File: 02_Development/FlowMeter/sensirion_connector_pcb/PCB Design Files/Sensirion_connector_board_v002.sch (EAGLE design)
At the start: 13 parts

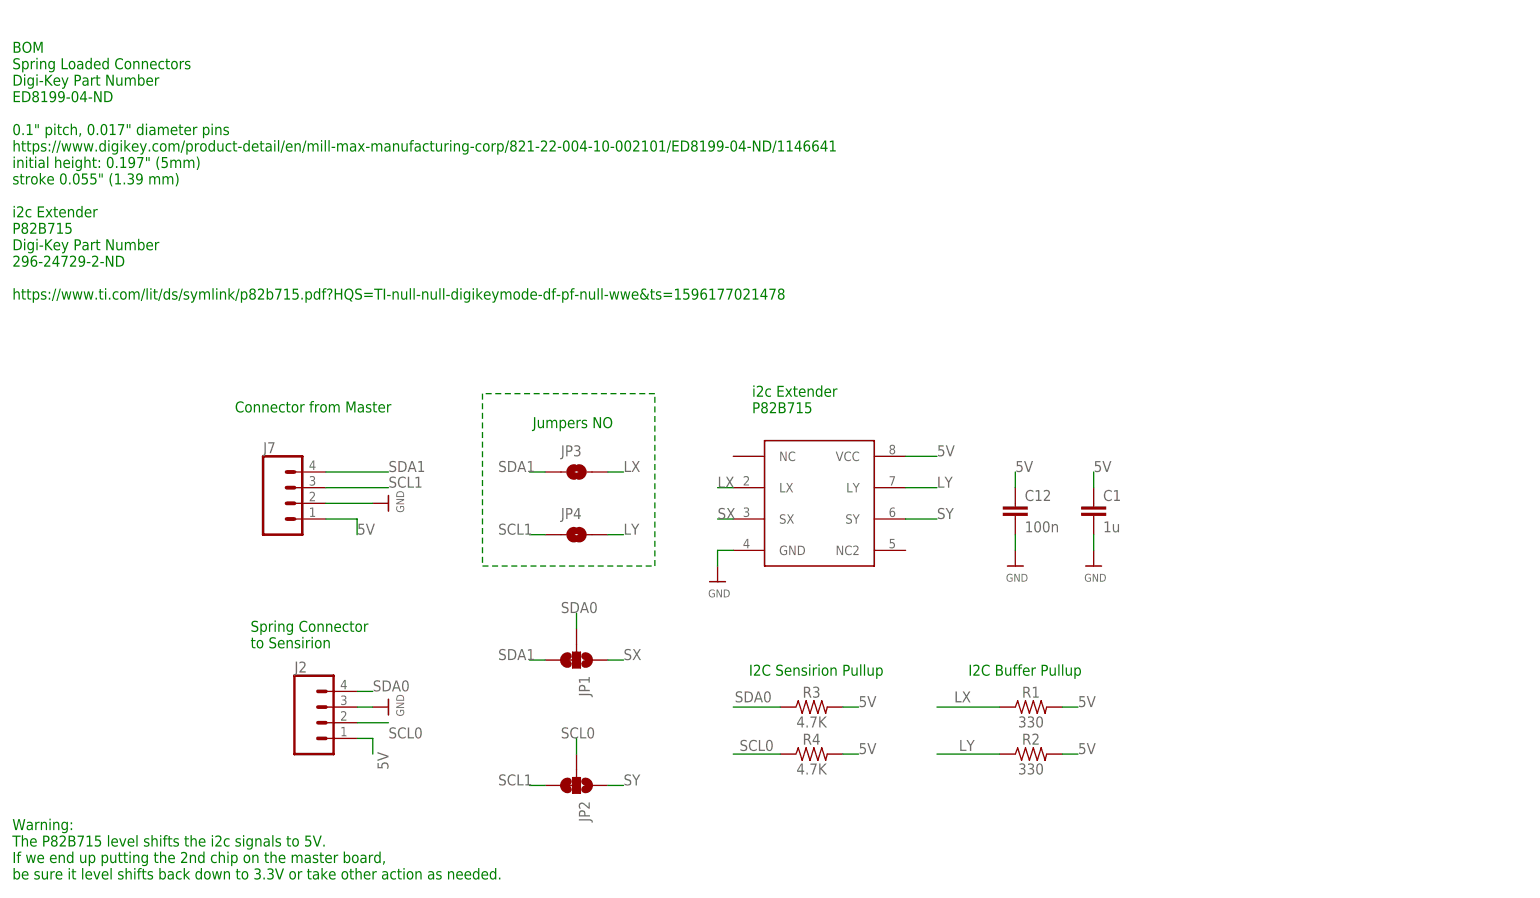
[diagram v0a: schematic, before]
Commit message: Added power jumper, redid all manufacturing files & BOMs
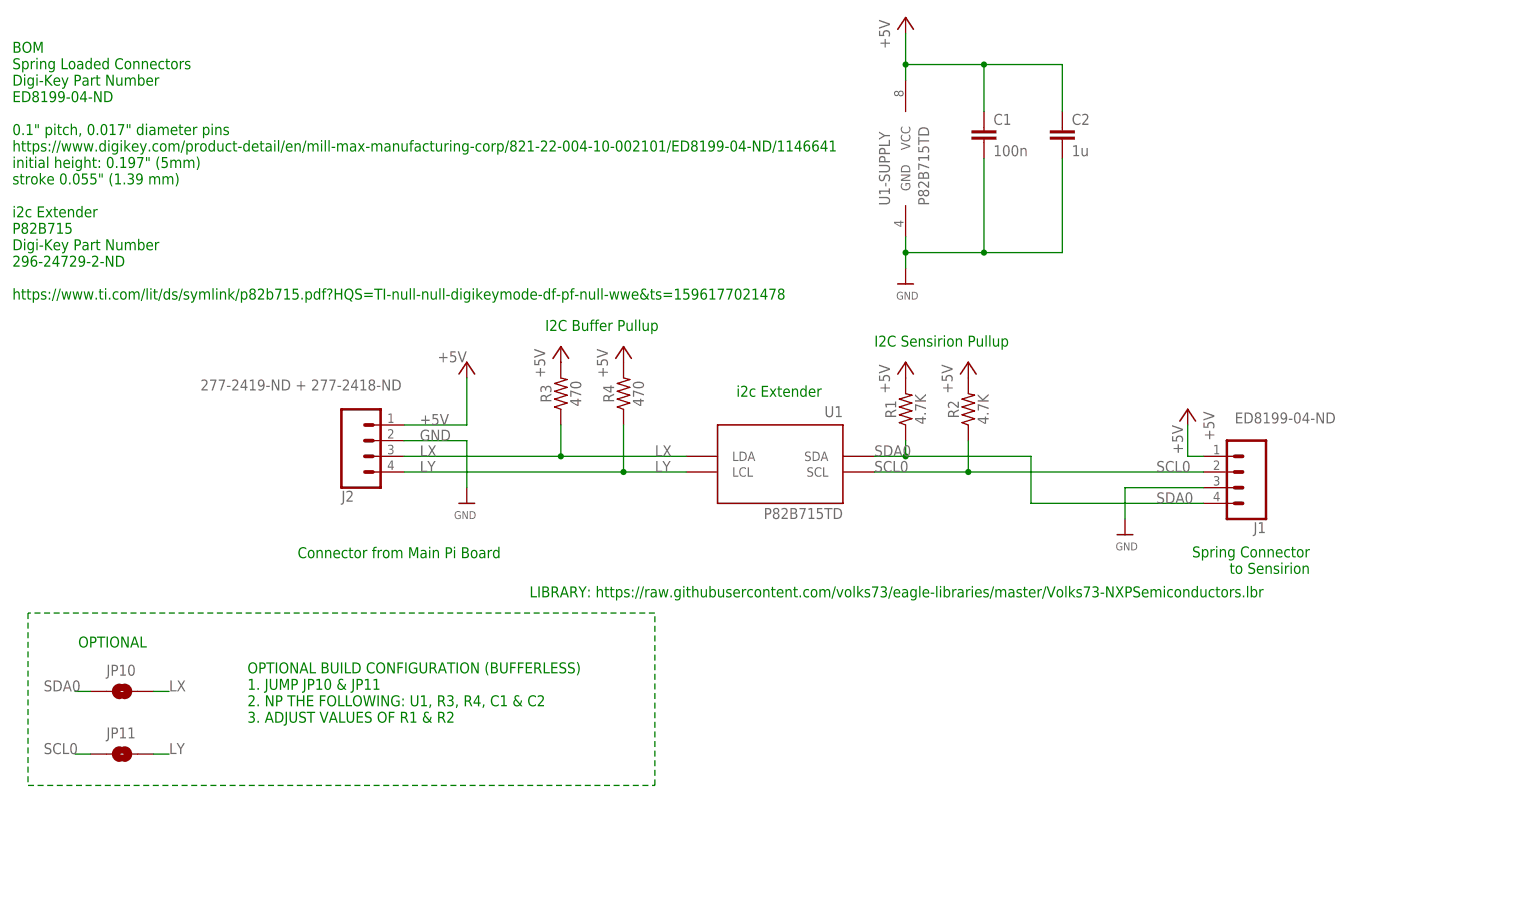
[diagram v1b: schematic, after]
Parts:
- removed C12: 100n, SparkFun-Capacitors:CAP-0805
- removed J7: (no value), th_libraries:CONN_043.5MM_RA
- removed JP1, JP2: JUMPER-SMT_3_1-NC_TRACE_NO-SILK, SparkFun-Jumpers:JUMPER-SMT_3_1-NC_TRACE_NO-SILK
- removed JP3, JP4: JUMPER-SMT_2_NO_SILK, SparkFun-Jumpers:JUMPER-SMT_2_NO_SILK
- removed U$2: P82B715, th_libraries:P82B715
- added C2: 1u, SparkFun-Capacitors:CAP-0805
- added J1: ED8199-04-ND, th_libraries:CONN_0430MILL_DIA
- added JP10, JP11: JUMPER-SMT_2_NO_SILK, SparkFun-Jumpers:JUMPER-SMT_2_NO_SILK
- added U1: P82B715TD, Volks73-NXPSemiconductors:P82B715TD
- C1: value 1u -> 100n
- J2: value (none) -> 277-2419-ND + 277-2418-ND; device th_libraries:CONN_0430MILL_DIA -> th_libraries:CONN_043.5MM_RA
- R1, R2: value 330 -> 4.7K
- R3, R4: value 4.7K -> 470
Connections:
- removed net 5V: C1.1, C12.1, J2.1, J7.1, R1.2, R2.2, R3.2, R4.2, U$2.VCC
- removed net SCL1: J7.3, JP2.3, JP4.1
- removed net SDA1: J7.4, JP1.3, JP3.1
- removed net SX: JP1.1, U$2.SX
- removed net SY: JP2.1, U$2.SY
- new net +5V: C1.1, C2.1, J1.1, J2.1, R1.2, R2.2, R3.2, R4.2, U1-SUPPLY.VCC
- net GND: now also C2.2, J1.3, J2.2, U1-SUPPLY.GND; no longer C12.2, J2.3, J7.2, U$2.GND
- net LX: now also J2.3, JP10.2, R3.1, U1U$1.LDA; no longer JP3.2, R1.1, U$2.LX
- net LY: now also J2.4, JP11.2, R4.1, U1U$1.LCL; no longer JP4.2, R2.1, U$2.LY
- net SCL0: now also J1.2, JP11.1, R2.1, U1U$1.SCL; no longer J2.2, JP2.2, R4.1
- net SDA0: now also J1.4, JP10.1, R1.1, U1U$1.SDA; no longer J2.4, JP1.2, R3.1
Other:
- note added: "Connector from Main Pi Board"
- note added: "LIBRARY: https://raw.githubusercontent.com/volks73/eagle-libraries/master/Volks73-NXPSemiconductors.lbr"
- note added: "OPTIONAL"
- note added: "OPTIONAL BUILD CONFIGURATION (BUFFERLESS) 1. JUMP JP10 & JP11 2. NP THE FOLLOWING: U1, R3, R4, C1 & C2 3. ADJUST VALUES OF R1 & R2"
- note added: "i2c Extender"
- note removed: "Connector from Master"
- note removed: "Jumpers NO"
- note removed: "Warning: The P82B715 level shifts the i2c signals to 5V. If we end up putting the 2nd chip on the master board, be sure it level shifts back down to 3.3V or take other action as needed."
- note removed: "i2c Extender P82B715"
- moved on the sheet: C1, J2, R1, R2, R3, R4
